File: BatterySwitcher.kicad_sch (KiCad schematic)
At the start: 2 parts

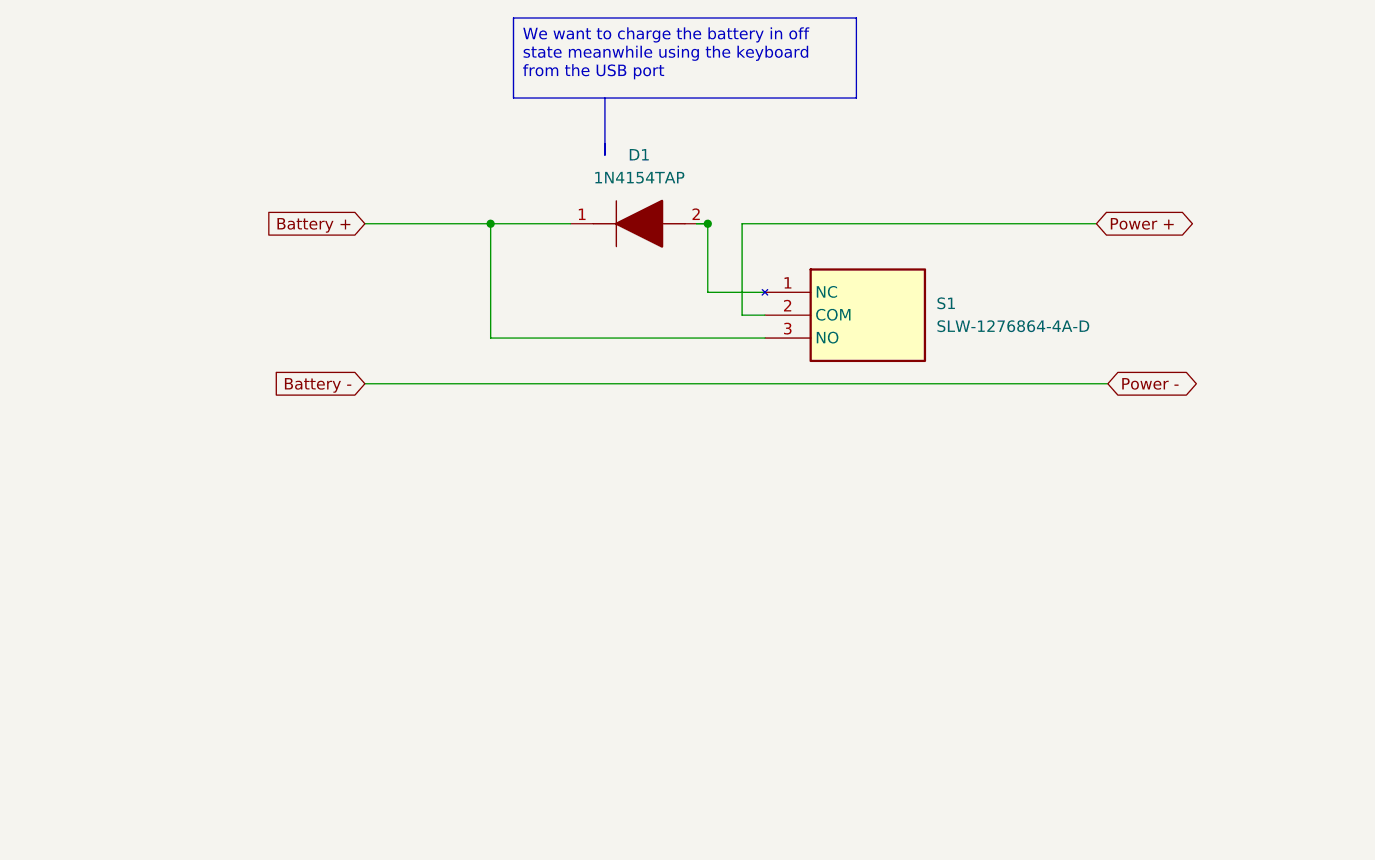
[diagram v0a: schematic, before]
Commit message: added dip pins for battery and power connections and routing done
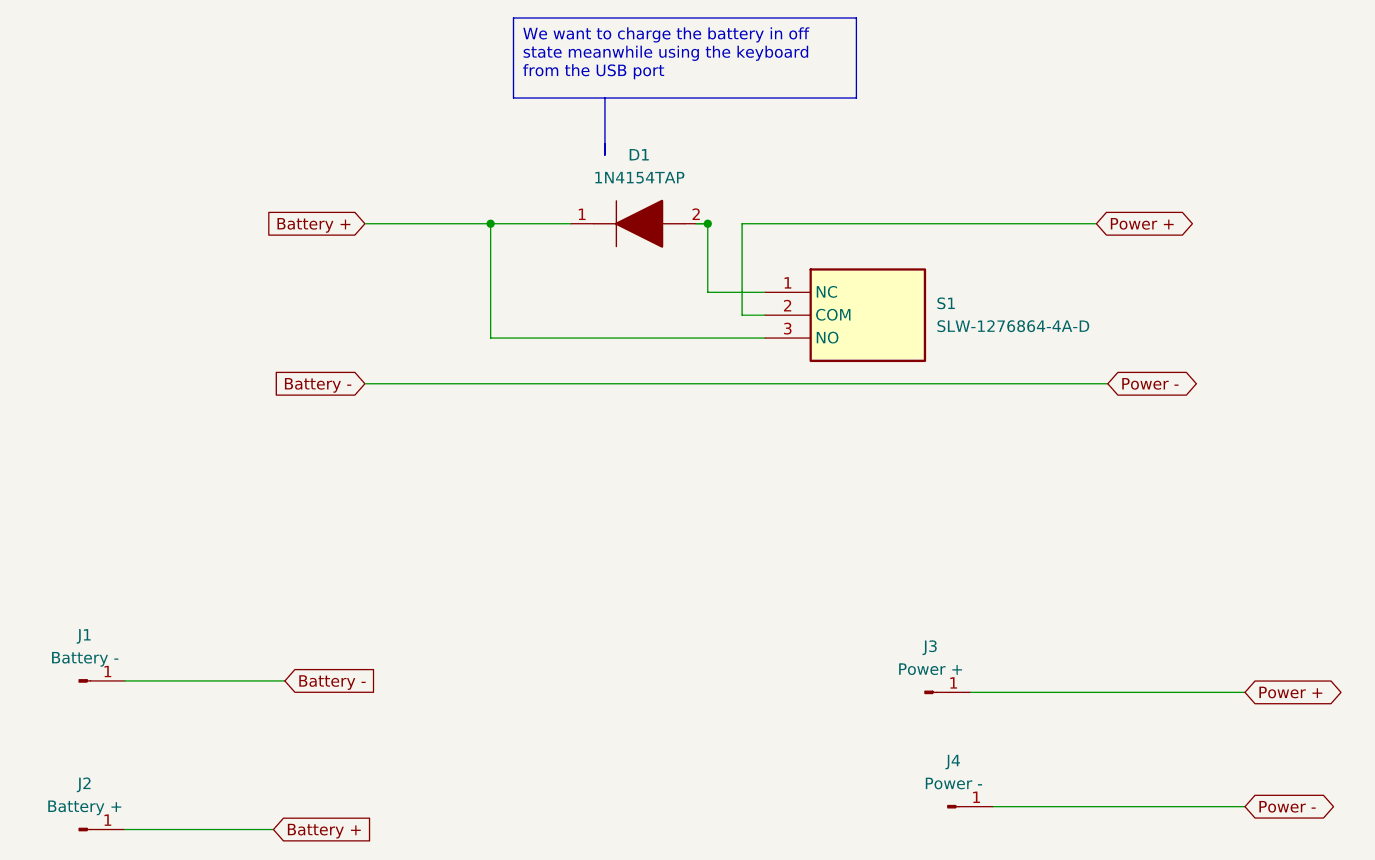
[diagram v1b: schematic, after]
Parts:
- added J1: Battery -, Connector_PinHeader_1.00mm:PinHeader_1x01_P1.00mm_Vertical, symbol Connector:Conn_01x01_Pin
- added J2: Battery +, Connector_PinHeader_1.00mm:PinHeader_1x01_P1.00mm_Vertical, symbol Connector:Conn_01x01_Pin
- added J3: Power +, Connector_PinHeader_1.00mm:PinHeader_1x01_P1.00mm_Vertical, symbol Connector:Conn_01x01_Pin
- added J4: Power -, Connector_PinHeader_1.00mm:PinHeader_1x01_P1.00mm_Vertical, symbol Connector:Conn_01x01_Pin
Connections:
- net Battery  +: now also J2.1 (Pin_1)
- net Battery  -: now also J1.1 (Pin_1), J4.1 (Pin_1)
- net Power  + : now also J3.1 (Pin_1)

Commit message: fixed some issues noticed from Miguel Angel
Removed ground plane
Checked copper width for 500mA
Changed diode to shottky with less forward voltage
Added battery connector
Rearrange header pins to be from behind
Reroute all
Added pcb measures
Added part number
Added my signature
Added bill of materials
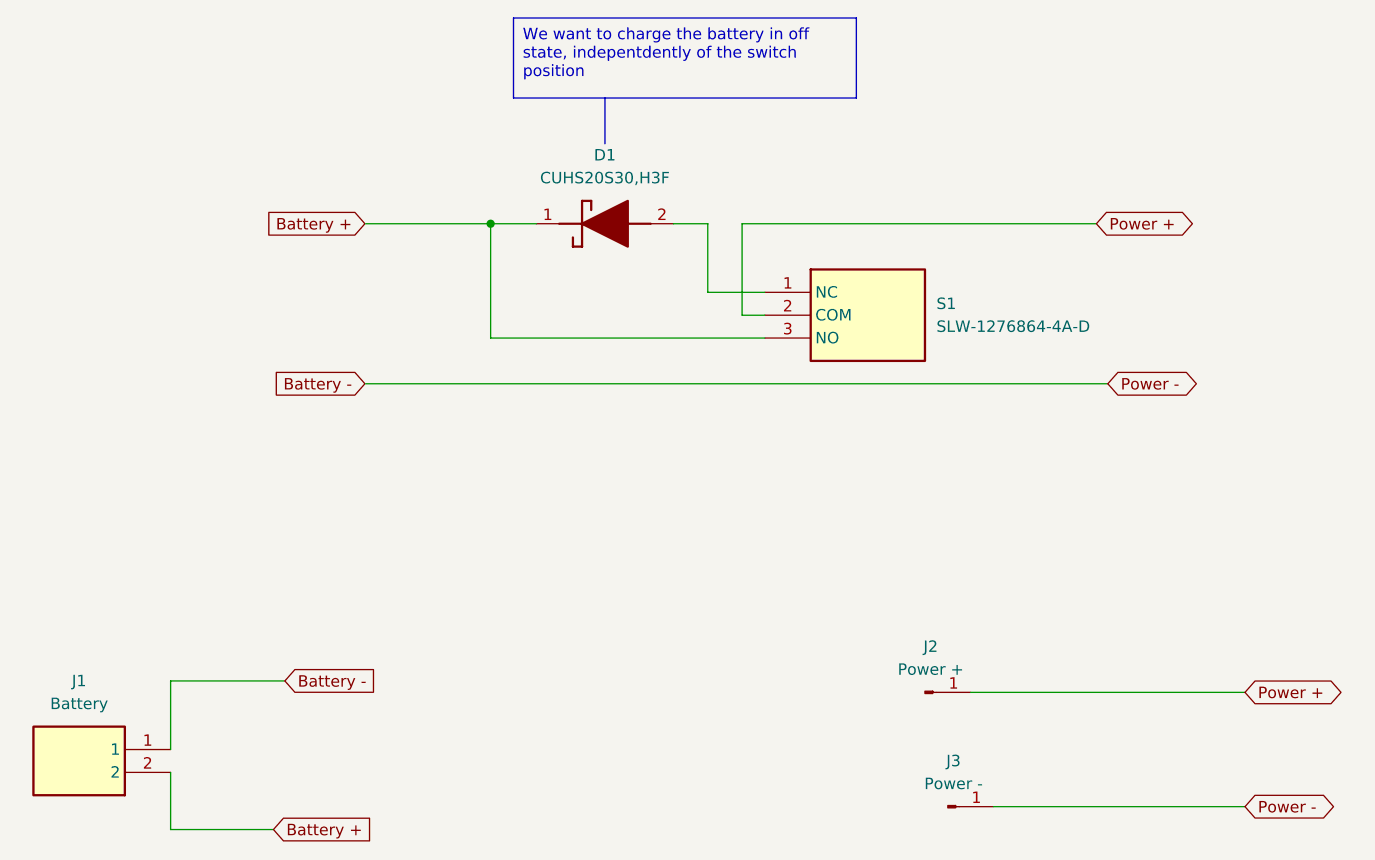
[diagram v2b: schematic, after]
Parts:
- removed D1: 1N4154TAP, DIOAD950W60L350D150, symbol 1N4154TAP:1N4154TAP
- removed J1: Battery -, Connector_PinHeader_1.00mm:PinHeader_1x01_P1.00mm_Vertical, symbol Connector:Conn_01x01_Pin
- removed J2: Battery +, Connector_PinHeader_1.00mm:PinHeader_1x01_P1.00mm_Vertical, symbol Connector:Conn_01x01_Pin
- added D1: CUHS20S30,H3F, SamacSys_Parts:CUHS20S40H3F, symbol SamacSys_Parts:CUHS20S30,H3F
- added J1: Battery, SamacSys_Parts:530470210, symbol SamacSys_Parts:53047-0210
- renumbered J3 to J2, J4 to J3
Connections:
- net Battery  +: now also D1.1 (K), J1.2
- net Battery  -: now also J1.1
- net at S1.1 (NC): now also D1.2 (A)

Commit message: changed switch by a shorter one
achieved minimum footprint
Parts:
- removed S1: SLW-1276864-4A-D, SLW12768644AD, symbol SLW-1276864-4A-D:SLW-1276864-4A-D
- added S1: SLW-883935-2A-D, SLW8839352AD, symbol SamacSys_Parts:SLW-883935-2A-D
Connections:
- net Battery  +: now also S1.3 (NO)
- net Power  + : now also S1.2 (COM)
- net at D1.2 (A): now also S1.1 (NC)
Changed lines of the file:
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@@
+	)
+	(symbol
+		(lib_id "SamacSys_Parts:SLW-883935-2A-D")
+		(at 130.81 64.77 0)
+		(unit 1)
+		(exclude_from_sim no)
+		(in_bom yes)
+		(on_board yes)
+		(dnp no)
+		(fields_autoplaced yes)
+		(property "Reference" "S1"
+			(at 149.86 66.0399 0)
+			(effects
+				(font
+					(size 1.27 1.27)
+				)
+				(justify left)
+			)
+		)
+		(property "Value" "SLW-883935-2A-D"
+			(at 149.86 68.5799 0)
+			(effects
+				(font
+					(size 1.27 1.27)
+				)
+				(justify left)
+			)
+		)
+		(property "Footprint" "SLW8839352AD"
+			(at 149.86 159.69 0)
+			(effects
+				(font
+					(size 1.27 1.27)
+				)
+				(justify left top)
+				(hide yes)
+			)
+		)
+		(property "Datasheet" "https://www.cuidevices.com/product/resource/pdf/slw-883935-2a-d.pdf"
+			(at 149.86 259.69 0)
+			(effects
+				(font
+					(size 1.27 1.27)
+				)
+				(justify left top)
+				(hide yes)
+			)
+		)
+		(property "Description" "Slide Switches 8.8 x 3.9 x 3.5 mm, 2 mm Raised Slide Actuator, Right-Angle, Through Hole"
+			(at 130.81 64.77 0)
+			(effects
+				(font
+					(size 1.27 1.27)
+				)
+				(hide yes)
+			)
+		)
+		(property "Height" "6.1"
+			(at 149.86 459.69 0)
+			(effects
+				(font
+					(size 1.27 1.27)
+				)
+				(justify left top)
+				(hide yes)
+			)
+		)
+		(property "Manufacturer_Name" "CUI Devices"
+			(at 149.86 559.69 0)
+			(effects
+				(font
+					(size 1.27 1.27)
+				)
+				(justify left top)
+				(hide yes)
+			)
+		)
+		(property "Manufacturer_Part_Number" "SLW-883935-2A-D"
+			(at 149.86 659.69 0)
+			(effects
+				(font
+					(size 1.27 1.27)
+				)
+				(justify left top)
+				(hide yes)
+			)
+		)
+		(property "Mouser Part Number" "179-SLW-883935-2A-D"
+			(at 149.86 759.69 0)
+			(effects
+				(font
+					(size 1.27 1.27)
+				)
+				(justify left top)
+				(hide yes)
+			)
+		)
+		(property "Mouser Price/Stock" "https://www.mouser.co.uk/ProductDetail/CUI-Devices/SLW-883935-2A-D?qs=1Kr7Jg1SGW%2Fv9j8ky6fn%2FQ%3D%3D"
+			(at 149.86 859.69 0)
+			(effects
+				(font
+					(size 1.27 1.27)
+				)
+				(justify left top)
+				(hide yes)
+			)
+		)
+		(property "Arrow Part Number" "SLW-883935-2A-D"
+			(at 149.86 959.69 0)
+			(effects
+				(font
+					(size 1.27 1.27)
+				)
+				(justify left top)
+				(hide yes)
+			)
+		)
+		(property "Arrow Price/Stock" "https://www.arrow.com/en/products/slw-883935-2a-d/cui-devices?region=nac"
+			(at 149.86 1059.69 0)
+			(effects
+				(font
+					(size 1.27 1.27)
+				)
+				(justify left top)
+				(hide yes)
+			)
+		)
+		(pin "2"
+		)
+		(pin "1"
+		)
+		(pin "3"
+		)
+		(instances
+			(project "BatterySwitcher"
+				(path "/fff52d9c-2593-4d64-8717-f098392b56b0"
+					(reference "S1")
+					(unit 1)
+				)
+			)
+		)
 	)
 	(symbol
@@
 					(unit 1)
 				)
-			)
-		)
-	)
-	(symbol
-		(lib_id "SLW-1276864-4A-D:SLW-1276864-4A-D")
-		(at 130.81 64.77 0)
-		(unit 1)
-		(exclude_from_sim no)
-		(in_bom yes)
-		(on_board yes)
-		(dnp no)
-		(fields_autoplaced yes)
-		(property "Reference" "S1"
-			(at 149.86 66.0399 0)
-			(effects
-				(font
-					(size 1.27 1.27)
-				)
-				(justify left)
-			)
-		)
-		(property "Value" "SLW-1276864-4A-D"
-			(at 149.86 68.5799 0)
-			(effects
-				(font
-					(size 1.27 1.27)
-				)
-				(justify left)
-			)
-		)
-		(property "Footprint" "SLW12768644AD"
-			(at 149.86 159.69 0)
-			(effects
-				(font
-					(size 1.27 1.27)
-				)
-				(justify left top)
-				(hide yes)
-			)
-		)
-		(property "Datasheet" "https://www.mouser.es/ProductDetail/CUI-Devices/SLW-1276864-4A-D?qs=1Kr7Jg1SGW90vOt02EYiag%3D%3D"
-			(at 149.86 259.69 0)
-			(effects
-				(font
-					(size 1.27 1.27)
-				)
-				(justify left top)
-				(hide yes)
-			)
-		)
-		(property "Description" "Slide Switches 12.7 x 6.8 x 6.4 mm, 2 mm Raised Slide Actuator, Vertical, Through Hole"
-			(at 130.81 64.77 0)
-			(effects
-				(font
-					(size 1.27 1.27)
-				)
-				(hide yes)
-			)
-		)
-		(property "Height" "10.6"
-			(at 149.86 459.69 0)
-			(effects
-				(font
-					(size 1.27 1.27)
-				)
-				(justify left top)
-				(hide yes)
-			)
-		)
-		(property "Mouser Part Number" "179-SLW-1276864-4A-D"
-			(at 149.86 559.69 0)
-			(effects
-				(font
-					(size 1.27 1.27)
-				)
-				(justify left top)
-				(hide yes)
-			)
-		)
-		(property "Mouser Price/Stock" "https://www.mouser.co.uk/ProductDetail/CUI-Devices/SLW-1276864-4A-D?qs=1Kr7Jg1SGW90vOt02EYiag%3D%3D"
-			(at 149.86 659.69 0)
-			(effects
-				(font
-					(size 1.27 1.27)
-				)
-				(justify left top)
-				(hide yes)
-			)
-		)
-		(property "Manufacturer_Name" "CUI Devices"
-			(at 149.86 759.69 0)
-			(effects
-				(font
-					(size 1.27 1.27)
-				)
-				(justify left top)
-				(hide yes)
-			)
-		)
-		(property "Manufacturer_Part_Number" "SLW-1276864-4A-D"
-			(at 149.86 859.69 0)
-			(effects
-				(font
-					(size 1.27 1.27)
-				)
-				(justify left top)
-				(hide yes)
-			)
-		)
-		(pin "2"
-		)
-		(pin "1"
-		)
-		(pin "3"
-		)
-		(instances
-			(project "BatterySwitcher"
-				(path "/fff52d9c-2593-4d64-8717-f098392b56b0"
-					(reference "S1")
-					(unit 1)
-				)

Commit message: finished development
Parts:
- removed D1: CUHS20S30,H3F, SamacSys_Parts:CUHS20S40H3F, symbol SamacSys_Parts:CUHS20S30,H3F
- removed J1: Battery, SamacSys_Parts:530470210, symbol SamacSys_Parts:53047-0210
- removed S1: SLW-883935-2A-D, SLW8839352AD, symbol SamacSys_Parts:SLW-883935-2A-D
- added D1: MBR0520LT1G, Samacsys:SOD3716X135N, symbol Samacsys:MBR0520LT1G
- added J1: 53047-0210, Samacsys:530470210, symbol Samacsys:53047-0210
- added S1: SS12D00G3, Samacsys:SS12D00G3, symbol Samacsys:SS12D00G3
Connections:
- net Battery  +: now also D1.1 (K), J1.2, S1.3 (NO)
- net Battery  -: now also J1.1
- net Power  + : now also S1.2 (COM)
- new net: D1.2 (A), S1.1 (NC)
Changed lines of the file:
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@@
 	)
 	(symbol
-		(lib_id "SamacSys_Parts:53047-0210")
+		(lib_id "Samacsys:53047-0210")
 		(at 64.77 118.11 180)
 		(unit 1)
@@
 			)
 		)
-		(property "Value" "Battery"
+		(property "Value" "53047-0210"
 			(at 54.61 110.49 0)
 			(effects
@@
 			)
 		)
-		(property "Footprint" "SamacSys_Parts:530470210"
+		(property "Footprint" "Samacsys:530470210"
 			(at 48.26 23.19 0)
 			(effects
@@
 			)
 		)
-		(property "Datasheet" "https://www.mouser.es/ProductDetail/Molex/53047-0210?qs=M5Ic86%252BuP8b8FQrTwriyOw%3D%3D"
+		(property "Datasheet" "https://componentsearchengine.com/Datasheets/2/53047-0210.pdf"
 			(at 48.26 -76.81 0)
 			(effects
@@
 			)
 		)
+		(pin "2"
+		)
 		(pin "1"
-		)
-		(pin "2"
 		)
 		(instances
@@
 	)
 	(symbol
-		(lib_id "SamacSys_Parts:CUHS20S30,H3F")
-		(at 102.87 57.15 0)
+		(lib_id "Samacsys:MBR0520LT1G")
+		(at 105.41 57.15 0)
 		(unit 1)
 		(exclude_from_sim no)
@@
 			)
 		)
-		(property "Value" "CUHS20S30,H3F"
+		(property "Value" "MBR0520LT1G"
 			(at 113.03 52.07 0)
 			(effects
@@
 			)
 		)
-		(property "Footprint" "SamacSys_Parts:CUHS20S40H3F"
-			(at 115.57 150.8 0)
-			(effects
-				(font
-					(size 1.27 1.27)
-				)
-				(justify left top)
-				(hide yes)
-			)
-		)
-		(property "Datasheet" "https://www.mouser.es/ProductDetail/Toshiba/CUHS20S30H3F?qs=PqoDHHvF64%252BnIC9Qnnw9zg%3D%3D"
-			(at 115.57 250.8 0)
-			(effects
-				(font
-					(size 1.27 1.27)
-				)
-				(justify left top)
-				(hide yes)
-			)
-		)
-		(property "Description" "Schottky Diodes & Rectifiers Sml-Signal Schottky 2A 30V 390pF"
-			(at 102.87 57.15 0)
-			(effects
-				(font
-					(size 1.27 1.27)
-				)
-				(hide yes)
-			)
-		)
-		(property "Height" ""
-			(at 115.57 450.8 0)
-			(effects
-				(font
-					(size 1.27 1.27)
-				)
-				(justify left top)
-				(hide yes)
-			)
-		)
-		(property "Manufacturer_Name" "Toshiba"
-			(at 115.57 550.8 0)
-			(effects
-				(font
-					(size 1.27 1.27)
-				)
-				(justify left top)
-				(hide yes)
-			)
-		)
-		(property "Manufacturer_Part_Number" "CUHS20S30,H3F"
-			(at 115.57 650.8 0)
-			(effects
-				(font
-					(size 1.27 1.27)
-				)
-				(justify left top)
-				(hide yes)
-			)
-		)
-		(property "Mouser Part Number" "757-CUHS20S30H3F"
-			(at 115.57 750.8 0)
-			(effects
-				(font
-					(size 1.27 1.27)
-				)
-				(justify left top)
-				(hide yes)
-			)
-		)
-		(property "Mouser Price/Stock" "https://www.mouser.co.uk/ProductDetail/Toshiba/CUHS20S30H3F?qs=PqoDHHvF64%252BnIC9Qnnw9zg%3D%3D"
-			(at 115.57 850.8 0)
-			(effects
-				(font
-					(size 1.27 1.27)
-				)
-				(justify left top)
-				(hide yes)
-			)
-		)
-		(property "Arrow Part Number" ""
-			(at 115.57 950.8 0)
-			(effects
-				(font
-					(size 1.27 1.27)
-				)
-				(justify left top)
-				(hide yes)
-			)
-		)
-		(property "Arrow Price/Stock" ""
-			(at 115.57 1050.8 0)
-			(effects
-				(font
-					(size 1.27 1.27)
-				)
-				(justify left top)
-				(hide yes)
-			)
+		(property "Footprint" "Samacsys:SOD3716X135N"
+			(at 116.84 154.61 0)
+			(effects
+				(font
+					(size 1.27 1.27)
+				)
+				(justify left top)
+				(hide yes)
+			)
+		)
+		(property "Datasheet" "http://www.onsemi.com/pub/Collateral/MBR0520LT1-D.PDF"
+			(at 116.84 254.61 0)
+			(effects
+				(font
+					(size 1.27 1.27)
+				)
+				(justify left top)
+				(hide yes)
+			)
+		)
+		(property "Description" "MBR0520LT1G, Schottky Diode,  0.5A max, 20V, 2-Pin, SOD-123"
+			(at 105.41 57.15 0)
+			(effects
+				(font
+					(size 1.27 1.27)
+				)
+				(hide yes)
+			)
+		)
+		(property "Height" "1.35"
+			(at 116.84 454.61 0)
+			(effects
+				(font
+					(size 1.27 1.27)
+				)
+				(justify left top)
+				(hide yes)
+			)
+		)
+		(property "Manufacturer_Name" "onsemi"
+			(at 116.84 554.61 0)
+			(effects
+				(font
+					(size 1.27 1.27)
+				)
+				(justify left top)
+				(hide yes)
+			)
+		)
+		(property "Manufacturer_Part_Number" "MBR0520LT1G"
+			(at 116.84 654.61 0)
+			(effects
+				(font
+					(size 1.27 1.27)
+				)
+				(justify left top)
+				(hide yes)
+			)
+		)
+		(property "Mouser Part Number" "863-MBR0520LT1G"
+			(at 116.84 754.61 0)
+			(effects
+				(font
+					(size 1.27 1.27)
+				)
+				(justify left top)
+				(hide yes)
+			)
+		)
+		(property "Mouser Price/Stock" "https://www.mouser.co.uk/ProductDetail/onsemi/MBR0520LT1G?qs=3JMERSakebqBWTiPUQp0nw%3D%3D"
+			(at 116.84 854.61 0)
+			(effects
+				(font
+					(size 1.27 1.27)
+				)
+				(justify left top)
+				(hide yes)
+			)
+		)
+		(property "Arrow Part Number" "MBR0520LT1G"
+			(at 116.84 954.61 0)
+			(effects
+				(font
+					(size 1.27 1.27)
+				)
+				(justify left top)
+				(hide yes)
+			)
+		)
+		(property "Arrow Price/Stock" "https://www.arrow.com/en/products/mbr0520lt1g/on-semiconductor?region=nac"
+			(at 116.84 1054.61 0)
+			(effects
+				(font
+					(size 1.27 1.27)
+				)
+				(justify left top)
+				(hide yes)
+			)
+		)
+		(pin "1"
 		)
 		(pin "2"
-		)
-		(pin "1"
 		)
 		(instances
@@
 	)
 	(symbol
-		(lib_id "SamacSys_Parts:SLW-883935-2A-D")
+		(lib_id "Samacsys:SS12D00G3")
 		(at 130.81 64.77 0)
 		(unit 1)
@@
 			)
 		)
-		(property "Value" "SLW-883935-2A-D"
+		(property "Value" "SS12D00G3"
 			(at 149.86 68.5799 0)
 			(effects
@@
 			)
 		)
-		(property "Footprint" "SLW8839352AD"
+		(property "Footprint" "Samacsys:SS12D00G3"
 			(at 149.86 159.69 0)
 			(effects
@@
 			)
 		)
-		(property "Datasheet" "https://www.cuidevices.com/product/resource/pdf/slw-883935-2a-d.pdf"
+		(property "Datasheet" "http://vimex.com/switches/techdocs/SS12D00-tech.pdf"
 			(at 149.86 259.69 0)
 			(effects
@@
 			)
 		)
-		(property "Description" "Slide Switches 8.8 x 3.9 x 3.5 mm, 2 mm Raised Slide Actuator, Right-Angle, Through Hole"
+		(property "Description" "3 Pin Toggle Switch"
 			(at 130.81 64.77 0)
 			(effects
@@
 			)
 		)
-		(property "Height" "6.1"
+		(property "Height" "7"
 			(at 149.86 459.69 0)
 			(effects
@@
 			)
 		)
-		(property "Manufacturer_Name" "CUI Devices"
+		(property "Manufacturer_Name" "Vimex"
 			(at 149.86 559.69 0)
 			(effects
@@
 			)
 		)
-		(property "Manufacturer_Part_Number" "SLW-883935-2A-D"
+		(property "Manufacturer_Part_Number" "SS12D00G3"
 			(at 149.86 659.69 0)
 			(effects
@@
 			)
 		)
-		(property "Mouser Part Number" "179-SLW-883935-2A-D"
+		(property "Mouser Part Number" ""
 			(at 149.86 759.69 0)
 			(effects
@@
 			)
 		)
-		(property "Mouser Price/Stock" "https://www.mouser.co.uk/ProductDetail/CUI-Devices/SLW-883935-2A-D?qs=1Kr7Jg1SGW%2Fv9j8ky6fn%2FQ%3D%3D"
+		(property "Mouser Price/Stock" ""
 			(at 149.86 859.69 0)
 			(effects
@@
 			)
 		)
-		(property "Arrow Part Number" "SLW-883935-2A-D"
+		(property "Arrow Part Number" ""
 			(at 149.86 959.69 0)
 			(effects
@@
 			)
 		)
-		(property "Arrow Price/Stock" "https://www.arrow.com/en/products/slw-883935-2a-d/cui-devices?region=nac"
+		(property "Arrow Price/Stock" ""
 			(at 149.86 1059.69 0)
 			(effects
@@
 			)
 		)
+		(pin "3"
+		)
 		(pin "2"
 		)
 		(pin "1"
 		)
-		(pin "3"
-		)
 		(instances
